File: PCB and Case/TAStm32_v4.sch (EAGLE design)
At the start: 37 parts, among them J1 ZX62D-B-5PA8, J10 RJSSE538002, J11 RJSSE538002, J12 SOICBITE, J13 CONSOLE_RESET, J2 UE27-AC54-100, J3 OLED128X64, J4 CONSOLE_RESET, J5 95278-802A12LF, J6 SAMTEC-TSM-106-01-X-SV_SAMTEC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, J7 SAMTEC-TSM-106-01-X-SV_SAMTEC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, J8 SAMTEC-TSM-106-01-X-SV_SAMTEC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, J9 SAMTEC-TSM-106-01-X-SV_SAMTEC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, U1 STM32F446RET6, U2 3.3V REG, Y1 8MHz

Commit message: 3D stuff
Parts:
- J10, J11: value RJSSE538002 -> RJSSE538002_RJSSE538002; device RJSSE538002:RJSSE538002 -> TAStm32_v4:RJSSE538002_RJSSE538002
- J13, J4: device TAStm32_v4:SAMTEC-TSM-102-01-X-SH_SAMTEC-TSM-102-01-X-SHJ -> TAStm32_v4:SAMTEC-TSM-102-01-X-SH_SAMTEC-TSM-102-01-X-SH
- J6, J7, J8, J9: value SAMTEC-TSM-106-01-X-SV_SAMTEC-TSM-106-01-X-SVJ -> SAMTEC-TSM-106-01-X-SV_SAMTEC-TSM-106-01-X-SV; device TAStm32_v4:SAMTEC-TSM-106-01-X-SV_SAMTEC-TSM-106-01-X-SVJ -> TAStm32_v4:SAMTEC-TSM-106-01-X-SV_SAMTEC-TSM-106-01-X-SV
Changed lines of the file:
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@@
 <part name="GND13" library="supply1" library_urn="urn:adsk.eagle:library:371" deviceset="GND" device=""/>
 <part name="J1" library="ZX62D-B-5PA8" deviceset="ZX62D-B-5PA8" device="" package3d_urn="urn:adsk.eagle:package:18856716/4"/>
-<part name="J10" library="RJSSE538002" deviceset="RJSSE538002" device="" package3d_urn="urn:adsk.eagle:package:18856791/2"/>
-<part name="J11" library="RJSSE538002" deviceset="RJSSE538002" device="" package3d_urn="urn:adsk.eagle:package:18856791/2"/>
-<part name="J4" library="TAStm32_v4" deviceset="SAMTEC-TSM-102-01-X-SH_SAMTEC-TSM-102-01-X-SH" device="J" value="CONSOLE_RESET"/>
-<part name="J6" library="TAStm32_v4" deviceset="SAMTEC-TSM-106-01-X-SV_SAMTEC-TSM-106-01-X-SV" device="J"/>
-<part name="J7" library="TAStm32_v4" deviceset="SAMTEC-TSM-106-01-X-SV_SAMTEC-TSM-106-01-X-SV" device="J"/>
-<part name="J8" library="TAStm32_v4" deviceset="SAMTEC-TSM-106-01-X-SV_SAMTEC-TSM-106-01-X-SV" device="J"/>
-<part name="J9" library="TAStm32_v4" deviceset="SAMTEC-TSM-106-01-X-SV_SAMTEC-TSM-106-01-X-SV" device="J"/>
-<part name="S1" library="3-1825910-1" deviceset="SWITCHN" device=""/>
-<part name="S2" library="3-1825910-1" deviceset="SWITCHN" device=""/>
-<part name="S3" library="3-1825910-1" deviceset="SWITCHN" device=""/>
-<part name="S4" library="3-1825910-1" deviceset="SWITCHN" device=""/>
-<part name="J2" library="SamacSys_Parts" deviceset="UE27-AC54-100" device=""/>
+<part name="J10" library="TAStm32_v4" deviceset="RJSSE538002_RJSSE538002" device="" package3d_urn="urn:adsk.eagle:package:18856791/2"/>
+<part name="J11" library="TAStm32_v4" deviceset="RJSSE538002_RJSSE538002" device="" package3d_urn="urn:adsk.eagle:package:18856791/2"/>
+<part name="J4" library="TAStm32_v4" deviceset="SAMTEC-TSM-102-01-X-SH_SAMTEC-TSM-102-01-X-SH" device="" package3d_urn="urn:adsk.eagle:package:18856692/2" value="CONSOLE_RESET"/>
+<part name="J6" library="TAStm32_v4" deviceset="SAMTEC-TSM-106-01-X-SV_SAMTEC-TSM-106-01-X-SV" device="" package3d_urn="urn:adsk.eagle:package:18856577/2"/>
+<part name="J7" library="TAStm32_v4" deviceset="SAMTEC-TSM-106-01-X-SV_SAMTEC-TSM-106-01-X-SV" device="" package3d_urn="urn:adsk.eagle:package:18856577/2"/>
+<part name="J8" library="TAStm32_v4" deviceset="SAMTEC-TSM-106-01-X-SV_SAMTEC-TSM-106-01-X-SV" device="" package3d_urn="urn:adsk.eagle:package:18856577/2"/>
+<part name="J9" library="TAStm32_v4" deviceset="SAMTEC-TSM-106-01-X-SV_SAMTEC-TSM-106-01-X-SV" device="" package3d_urn="urn:adsk.eagle:package:18856577/2"/>
+<part name="S1" library="3-1825910-1" deviceset="SWITCHN" device="" override_package3d_urn="urn:adsk.eagle:package:25997948/2" override_package_urn="urn:adsk.eagle:footprint:25997949/1"/>
+<part name="S2" library="3-1825910-1" deviceset="SWITCHN" device="" override_package3d_urn="urn:adsk.eagle:package:25998021/2" override_package_urn="urn:adsk.eagle:footprint:25998023/1"/>
+<part name="S3" library="3-1825910-1" deviceset="SWITCHN" device="" override_package3d_urn="urn:adsk.eagle:package:25998025/2" override_package_urn="urn:adsk.eagle:footprint:25998026/1"/>
+<part name="S4" library="3-1825910-1" deviceset="SWITCHN" device="" override_package3d_urn="urn:adsk.eagle:package:25998028/2" override_package_urn="urn:adsk.eagle:footprint:25998029/1"/>
+<part name="J2" library="SamacSys_Parts" deviceset="UE27-AC54-100" device="" override_package3d_urn="urn:adsk.eagle:package:25997941/2" override_package_urn="urn:adsk.eagle:footprint:25997942/1"/>
 <part name="D1" library="TAStm32_v4" deviceset="DIODE_BAT60J" device="" value="BAT60J"/>
 <part name="D2" library="TAStm32_v4" deviceset="DIODE_BAT60J" device="" value="BAT60J"/>
@@
 <part name="U1" library="TAStm32_v4" deviceset="STM32F446RET6_STM32F446RET6" device="" value="STM32F446RET6"/>
 <part name="FRAME1" library="frames" library_urn="urn:adsk.eagle:library:229" deviceset="A4L-LOC" device=""/>
-<part name="Y1" library="TAStm32_v4" deviceset="ABMM-8.000MHZ-B2-T_ABMM-8.000MHZ-B2-T" device="" value="8MHz"/>
+<part name="Y1" library="TAStm32_v4" deviceset="ABMM-8.000MHZ-B2-T_ABMM-8.000MHZ-B2-T" device="" package3d_urn="urn:adsk.eagle:package:18857024/2" value="8MHz"/>
 <part name="GND6" library="supply1" library_urn="urn:adsk.eagle:library:371" deviceset="GND" device=""/>
 <part name="GND4" library="supply1" library_urn="urn:adsk.eagle:library:371" deviceset="GND" device=""/>
-<part name="J3" library="TAStm32_v4" deviceset="OLED128X64" device=""/>
+<part name="J3" library="TAStm32_v4" deviceset="OLED128X64" device="" override_package3d_urn="urn:adsk.eagle:package:25996617/2" override_package_urn="urn:adsk.eagle:footprint:25996642/1"/>
 <part name="J12" library="SOICbite_Eagle" deviceset="SOICBITE" device="" override_package3d_urn="urn:adsk.eagle:package:18876678/2" override_package_urn="urn:adsk.eagle:footprint:18876679/1"/>
-<part name="J5" library="SamacSys_Parts" deviceset="95278-802A12LF" device=""/>
+<part name="J5" library="SamacSys_Parts" deviceset="95278-802A12LF" device="" override_package3d_urn="urn:adsk.eagle:package:25996222/2" override_package_urn="urn:adsk.eagle:footprint:25996223/1"/>
 <part name="U2" library="linear" library_urn="urn:adsk.eagle:library:262" deviceset="MC33269ST*" device="" package3d_urn="urn:adsk.eagle:package:28541/2" technology="-3.3T3" value="3.3V REG"/>
 <part name="SUPPLY5" library="supply2" library_urn="urn:adsk.eagle:library:372" deviceset="V+" device=""/>
@@
 <part name="SUPPLY10" library="supply2" library_urn="urn:adsk.eagle:library:372" deviceset="V+" device=""/>
 <part name="SUPPLY11" library="supply2" library_urn="urn:adsk.eagle:library:372" deviceset="V+" device=""/>
-<part name="J13" library="TAStm32_v4" deviceset="SAMTEC-TSM-102-01-X-SH_SAMTEC-TSM-102-01-X-SH" device="J" value="CONSOLE_RESET"/>
+<part name="J13" library="TAStm32_v4" deviceset="SAMTEC-TSM-102-01-X-SH_SAMTEC-TSM-102-01-X-SH" device="" package3d_urn="urn:adsk.eagle:package:18856692/2" value="CONSOLE_RESET"/>
 </parts>
 <sheets>

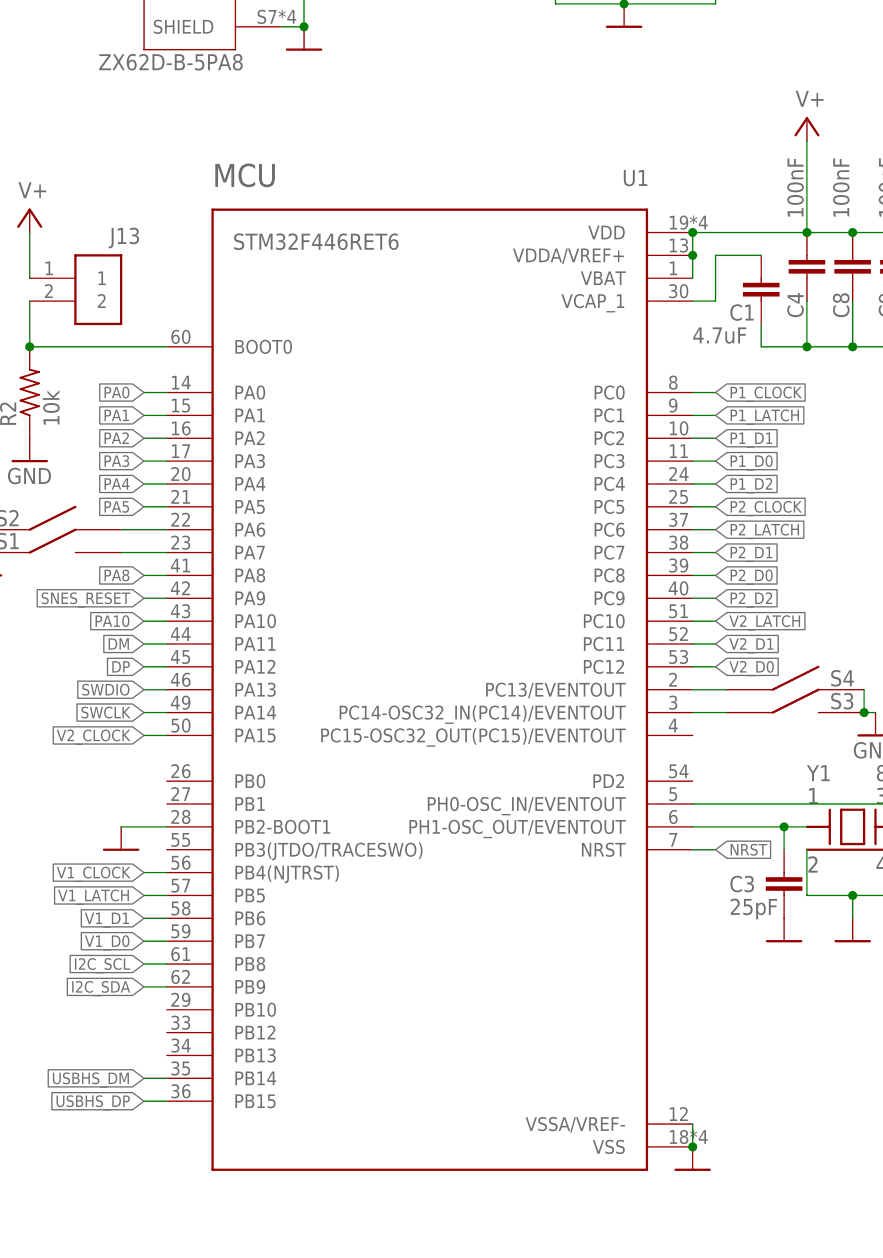
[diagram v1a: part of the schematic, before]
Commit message: 3D packages
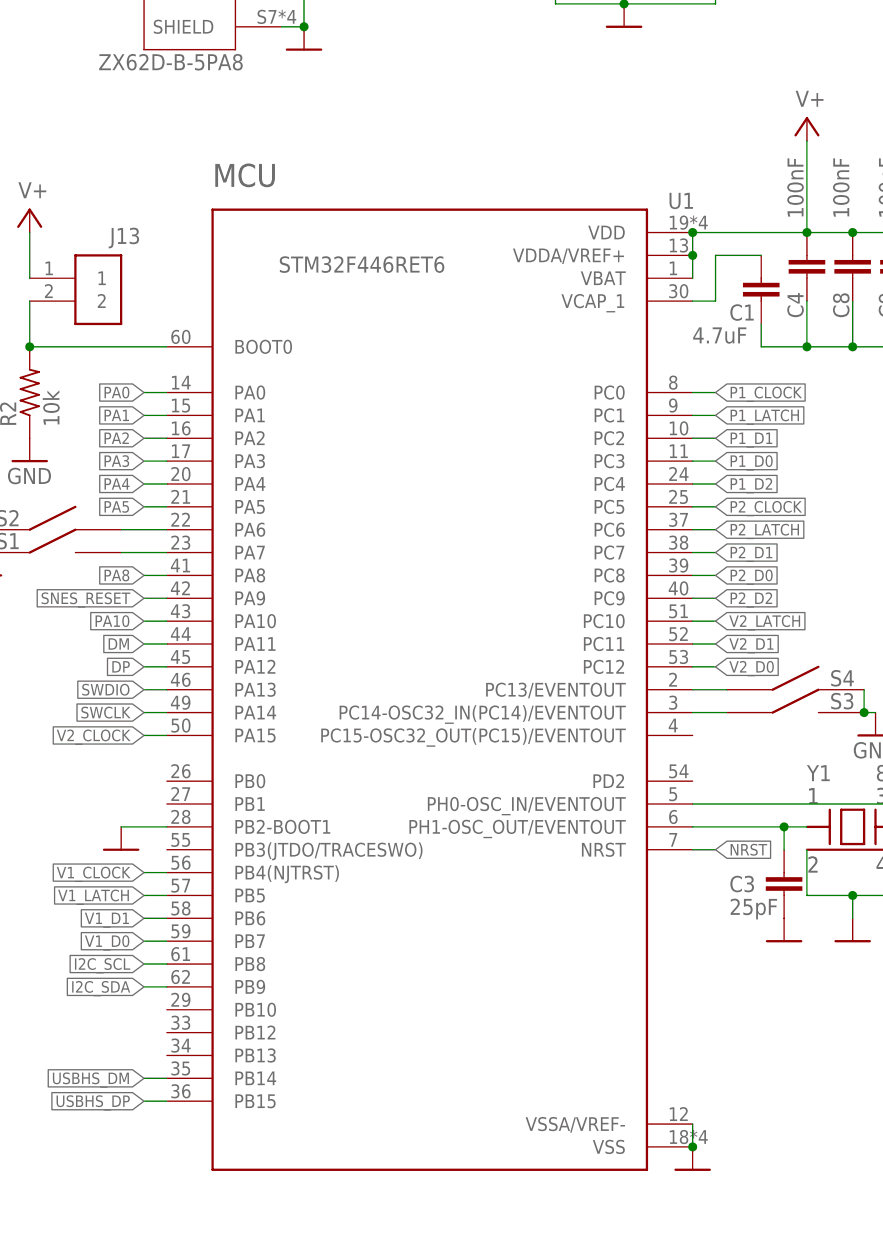
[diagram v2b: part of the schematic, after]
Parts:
- U1: device TAStm32_v4:STM32F446RET6_STM32F446RET6 -> STM32F446RET6:STM32F446RET7
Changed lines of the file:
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@@
 <part name="GND5" library="supply1" library_urn="urn:adsk.eagle:library:371" deviceset="GND" device=""/>
 <part name="SUPPLY7" library="supply2" library_urn="urn:adsk.eagle:library:372" deviceset="+5V" device=""/>
-<part name="U1" library="TAStm32_v4" deviceset="STM32F446RET6_STM32F446RET6" device="" value="STM32F446RET6"/>
+<part name="U1" library="STM32F446RET6" deviceset="STM32F446RET7" device="" package3d_urn="urn:adsk.eagle:package:18856813/2" value="STM32F446RET6"/>
 <part name="FRAME1" library="frames" library_urn="urn:adsk.eagle:library:229" deviceset="A4L-LOC" device=""/>
 <part name="Y1" library="TAStm32_v4" deviceset="ABMM-8.000MHZ-B2-T_ABMM-8.000MHZ-B2-T" device="" package3d_urn="urn:adsk.eagle:package:18857024/2" value="8MHz"/>
@@
 <attribute name="VALUE" x="3.175" y="79.375" size="1.778" layer="96"/>
 </instance>
-<instance part="U1" gate="G$1" x="-93.98" y="-10.16" smashed="yes">
-<attribute name="NAME" x="-71.341" y="43.2727" size="1.778" layer="95"/>
-<attribute name="VALUE" x="-114.598" y="37.9688" size="1.78216875" layer="96" rot="MR180"/>
+<instance part="U1" gate="G$1" x="-88.9" y="-12.7" smashed="yes">
+<attribute name="NAME" x="-66.261" y="40.7327" size="1.778" layer="95"/>
+<attribute name="VALUE" x="-109.518" y="35.4288" size="1.78216875" layer="96" rot="MR180"/>
 </instance>
 <instance part="FRAME1" gate="G$1" x="-149.86" y="-83.82" smashed="yes">

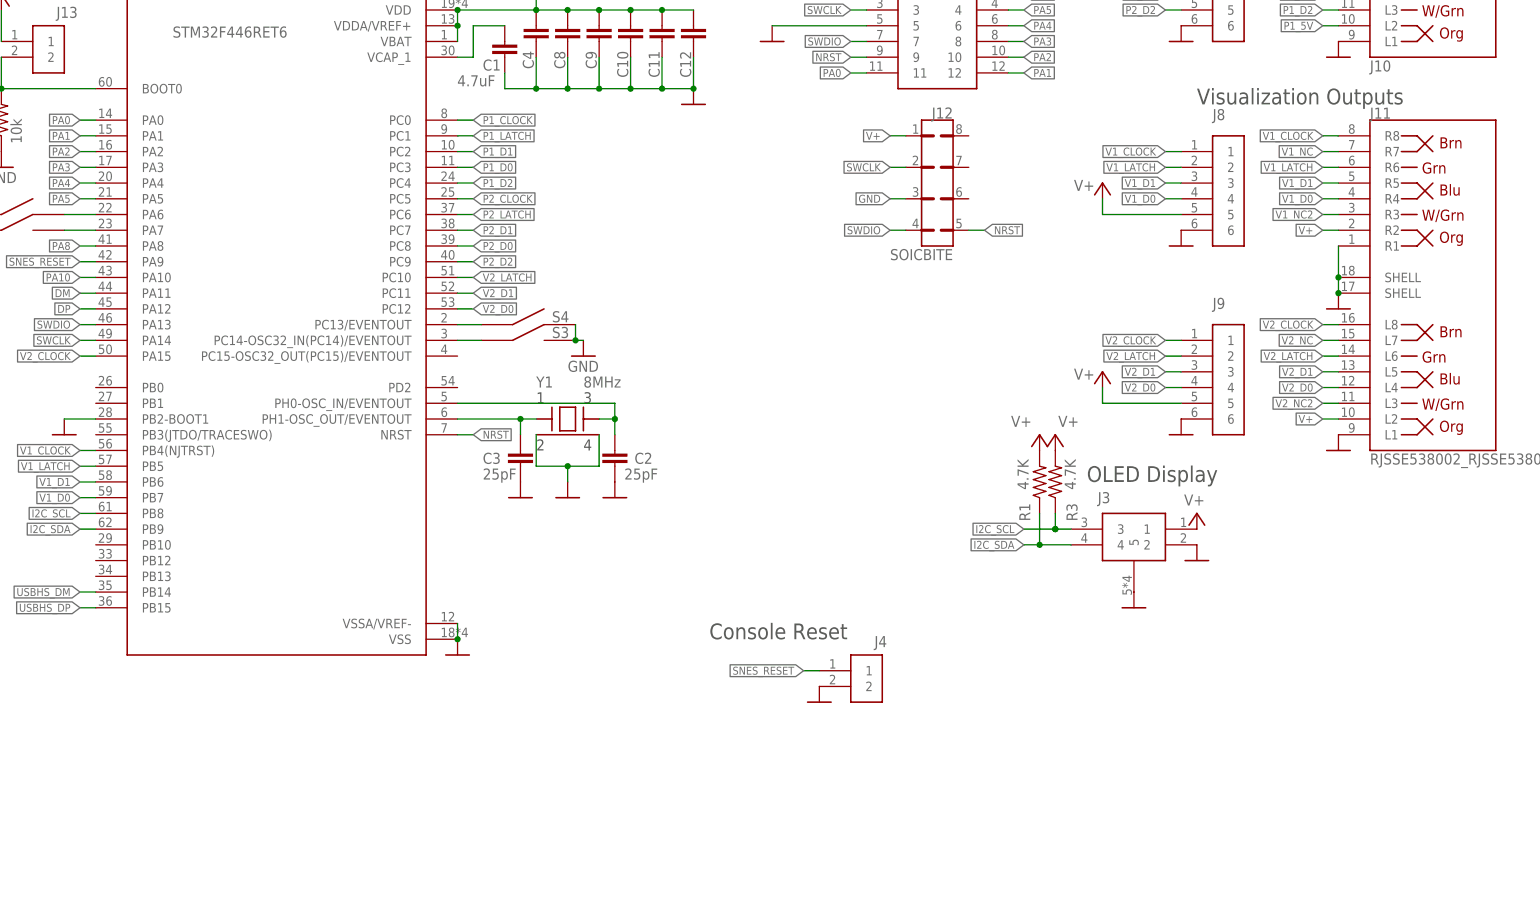
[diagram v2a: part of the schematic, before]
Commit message: Started adding level translators
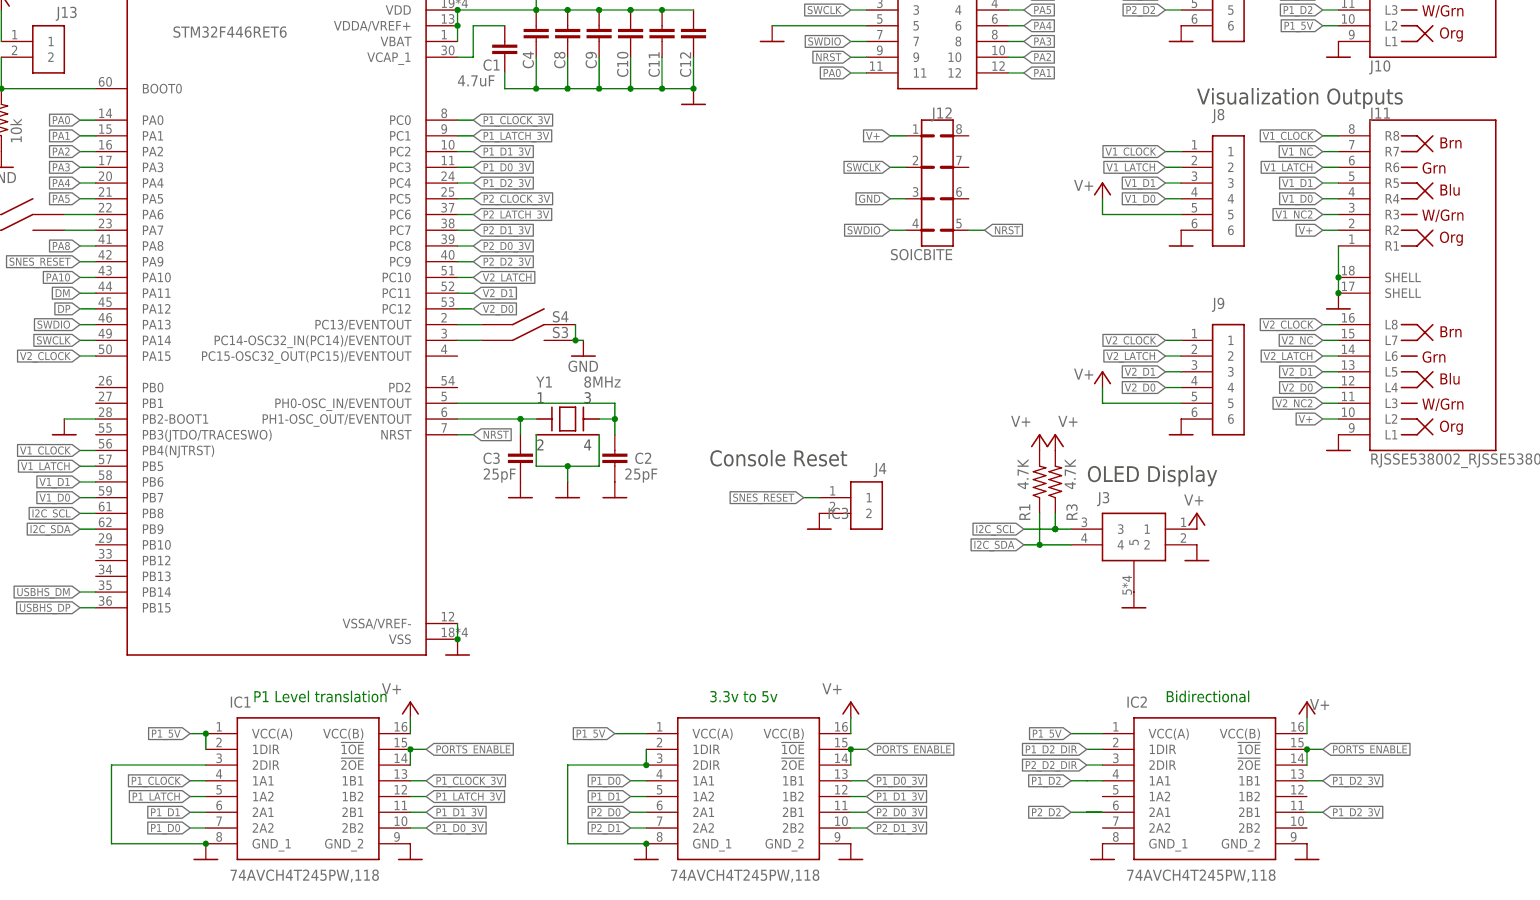
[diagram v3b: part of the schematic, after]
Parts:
- added IC1, IC2, IC3: 74AVCH4T245PW,118, SamacSys_Parts:74AVCH4T245PW,118
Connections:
- new net N$11: IC2.2A1
- new net N$9: IC2.1A1
- new net P1_CLOCK_3V: IC1.1B1, U1.PC0
- new net P1_D0_3V: IC1.2B2, IC3.1B1, U1.PC3
- new net P1_D1_3V: IC1.2B1, IC3.1B2, U1.PC2
- new net P1_D2_3V: IC2.1B1, IC2.2B1, U1.PC4
- new net P1_D2_DIR: IC2.1DIR
- new net P1_LATCH_3V: IC1.1B2, U1.PC1
- new net P2_CLOCK_3V: U1.PC5
- new net P2_D0_3V: IC3.2B1, U1.PC8
- new net P2_D1_3V: IC3.2B2, U1.PC7
- new net P2_D2_3V: U1.PC9
- new net P2_D2_DIR: IC2.2DIR
- new net P2_LATCH_3V: U1.PC6
- new net PORTS_ENABLE: IC1.!1OE, IC1.!2OE, IC2.!1OE, IC2.!2OE, IC3.!1OE, IC3.!2OE
- net GND: now also IC1.2DIR, IC1.GND_1, IC1.GND_2, IC2.GND_1, IC2.GND_2, IC3.1DIR, IC3.2DIR, IC3.GND_1, IC3.GND_2
- net P1_5V: now also IC1.1DIR, IC1.VCC(A), IC2.VCC(A), IC3.VCC(A)
- net P1_CLOCK: now also IC1.1A1; no longer U1.PC0
- net P1_D0: now also IC1.2A2, IC3.1A1; no longer U1.PC3
- net P1_D1: now also IC1.2A1, IC3.1A2; no longer U1.PC2
- net P1_D2: no longer U1.PC4
- net P1_LATCH: now also IC1.1A2; no longer U1.PC1
- net P2_CLOCK: no longer U1.PC5
- net P2_D0: now also IC3.2A1; no longer U1.PC8
- net P2_D1: now also IC3.2A2; no longer U1.PC7
- net P2_D2: no longer U1.PC9
- net P2_LATCH: no longer U1.PC6
- net V+: now also IC1.VCC(B), IC2.VCC(B), IC3.VCC(B)
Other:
- note added: "3.3v to 5v"
- note added: "Bidirectional"
- note added: "P1 Level translation"
- moved on the sheet: J4

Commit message: added note
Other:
- note added: "4=pin header is totally wrong, pins are staggered on the wrong size"
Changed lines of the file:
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@@
 <text x="-22.86" y="-73.66" size="1.778" layer="91">3.3v to 5v</text>
 <text x="50.8" y="-73.66" size="1.778" layer="91">Bidirectional</text>
+<text x="17.78" y="-60.96" size="1.778" layer="91">4=pin header is totally wrong, pins are staggered on the wrong size</text>
 </plain>
 <instances>

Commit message: More notes
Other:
- note added: "4=pin header is totally wrong, pins are staggered on the wrong side"
- note added: "Buffer SNES pin"
- note added: "Ground a pin for version number"
- note added: "Switch pinout wrong"
- note removed: "4=pin header is totally wrong, pins are staggered on the wrong size"
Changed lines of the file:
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@@
 <text x="-22.86" y="-73.66" size="1.778" layer="91">3.3v to 5v</text>
 <text x="50.8" y="-73.66" size="1.778" layer="91">Bidirectional</text>
-<text x="17.78" y="-60.96" size="1.778" layer="91">4=pin header is totally wrong, pins are staggered on the wrong size</text>
+<text x="17.78" y="-60.96" size="1.778" layer="91">4=pin header is totally wrong, pins are staggered on the wrong side</text>
+<text x="17.78" y="-63.5" size="1.778" layer="91">Buffer SNES pin</text>
+<text x="17.78" y="-66.04" size="1.778" layer="91">Switch pinout wrong</text>
+<text x="17.78" y="-68.58" size="1.778" layer="91">Ground a pin for version number</text>
 </plain>
 <instances>
@@
 <instance part="GND7" gate="1" x="-53.34" y="-40.64" smashed="yes"/>
 <instance part="C2" gate="G$1" x="-38.1" y="-35.56" smashed="yes" rot="R180">
-<attribute name="NAME" x="-32.004" y="-33.401" size="1.778" layer="95" rot="R180"/>
+<attribute name="NAME" x="-34.036" y="-35.179" size="1.778" layer="95"/>
 <attribute name="VALUE" x="-36.576" y="-37.719" size="1.778" layer="96"/>
 </instance>
@@
 </instance>
 <instance part="IC3" gate="G$1" x="-33.02" y="-78.74" smashed="yes">
-<attribute name="NAME" x="-3.81" y="-43.18" size="1.778" layer="95" align="center-left"/>
+<attribute name="NAME" x="-31.75" y="-73.66" size="1.778" layer="95" align="center-left"/>
 <attribute name="VALUE" x="-29.21" y="-101.6" size="1.778" layer="96" align="center-left"/>
 </instance>
